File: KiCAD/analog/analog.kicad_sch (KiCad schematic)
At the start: 0 parts

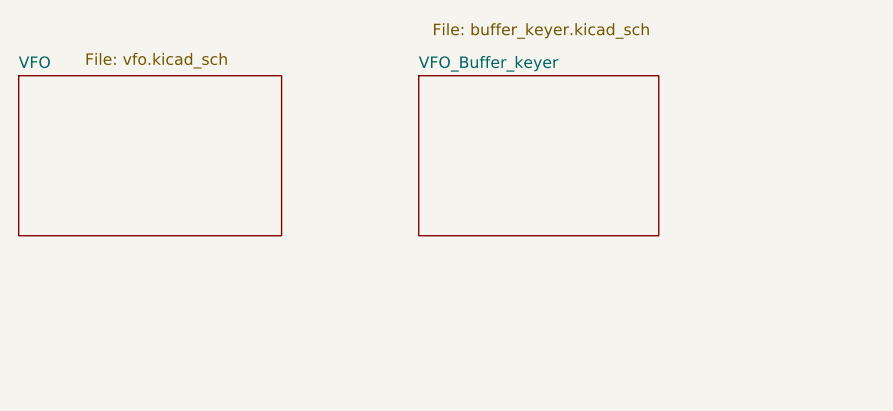
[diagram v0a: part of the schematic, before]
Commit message: KiCad revB: remove obsolete VFO sheets, add J3 footprint, add datasheets
- analog.kicad_sch: dropped VFO and VFO_Buffer_keyer sheets (legacy
  stubs superseded by VFO_Complete). Underlying vfo.kicad_sch and
  buffer_keyer.kicad_sch files deleted. PCB and .kicad_pro refreshed
  to match after Update PCB from Schematic.
- vfo_complete.kicad_sch: J3 (AC input to the +/-12V bridge) gets
  Phoenix Contact MKDS 1,5/2 footprint and a link to the local
  datasheet copy.
- Documentation/Components/: local datasheet copies for parts in the
  current supply bring-up (LM317L, LT1054, LM7800 series, 1N5817,
  2N3904/6, Kemet MLCC leaded, Phoenix Contact 142RHS).
- Documentation/Capacitors_Ordered.xlsx: capacitor inventory summary
  compiled from the Mouser and Digi-Key invoices, for stock-consistent
  reordering.

Co-Authored-By: Claude Opus 4.7 <noreply@anthropic.com>
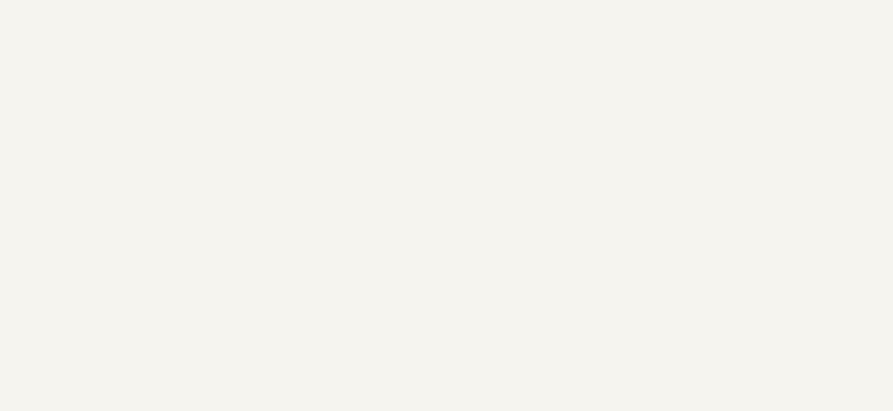
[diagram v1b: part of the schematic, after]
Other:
- removed sheet VFO
- removed sheet VFO_Buffer_keyer
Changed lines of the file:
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@@
-		)
-	)
-	(sheet
-		(at 74.93 41.91)
-		(size 26.67 17.78)
-		(exclude_from_sim no)
-		(in_bom yes)
-		(on_board yes)
-		(dnp no)
-		(stroke
-			(width 0.1524)
-			(type solid)
-		)
-		(fill
-			(color 0 0 0 0)
-		)
-		(property "Sheetname" "VFO_Buffer_keyer"
-			(at 74.93 41.1984 0)
-			(show_name no)
-			(do_not_autoplace no)
-			(effects
-				(font
-					(size 1.27 1.27)
-				)
-				(justify left bottom)
-			)
-		)
-		(property "Sheetfile" "buffer_keyer.kicad_sch"
-			(at 76.454 36.068 0)
-			(show_name no)
-			(do_not_autoplace no)
-			(effects
-				(font
-					(size 1.27 1.27)
-				)
-				(justify left top)
-			)
-		)
-		(instances
-			(project "analog"
-				(path "/d3de40b8-856b-4fbd-829c-f45ffcd55742"
-					(page "4")
-				)
-			)
-		)
-	)
-	(sheet
-		(at 30.48 41.91)
-		(size 29.21 17.78)
-		(exclude_from_sim no)
-		(in_bom yes)
-		(on_board yes)
-		(dnp no)
-		(stroke
-			(width 0.1524)
-			(type solid)
-		)
-		(fill
-			(color 0 0 0 0)
-		)
-		(property "Sheetname" "VFO"
-			(at 30.48 41.1984 0)
-			(show_name no)
-			(do_not_autoplace no)
-			(effects
-				(font
-					(size 1.27 1.27)
-				)
-				(justify left bottom)
-			)
-		)
-		(property "Sheetfile" "vfo.kicad_sch"
-			(at 37.846 39.37 0)
-			(show_name no)
-			(do_not_autoplace no)
-			(effects
-				(font
-					(size 1.27 1.27)
-				)
-				(justify left top)
-			)
-		)
-		(instances
-			(project "analog"
-				(path "/d3de40b8-856b-4fbd-829c-f45ffcd55742"
-					(page "3")
-				)
-			)
 		)
 	)

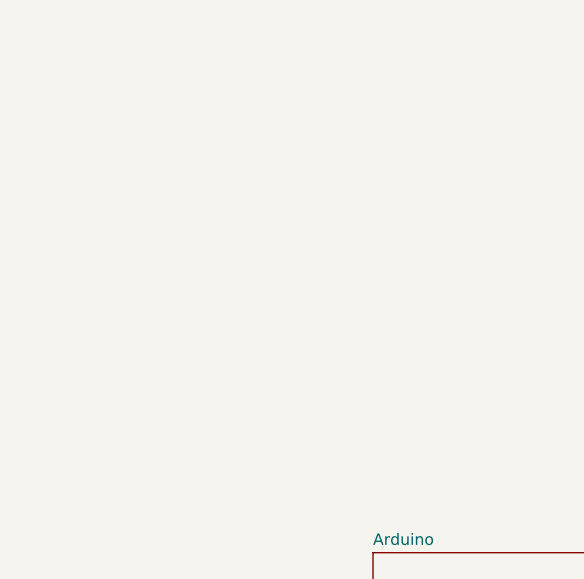
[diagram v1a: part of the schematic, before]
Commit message: revB frozen state: MCP4922 swap + LDAC decouple + sheet rename + protoshield work
Captures the in-flight state of revB at the point where the project pivoted
to a full-SS output stage on a new branch (SS_Rev_C, cut from this commit).
revB is retained as a fallback if the SS PA plan on revC proves inadequate.

Included changes:
- Analog: MCP4921 (single DAC) replaced with MCP4922 (dual DAC). Channel
  assignment: DAC_A -> PA_OUTPUT_LEVEL (new global label, awaiting PA
  board), DAC_B -> Gate 2 (DGFET envelope keyer). Channels swapped from
  initial-design intent for layout convenience.
- Analog: DAC_LDAC_N decoupled from PCF8575 P5 (that global label renamed
  to PCF_P5_SPARE). Intent: route LDAC to Metro A4 for zero-latency
  simultaneous-DAC-update capability. Physical route to A4 NOT yet added
  -- DAC_LDAC_N label on dac.kicad_sch is dangling and will fail ERC.
- Analog: KiCad-driven used_designators bookkeeping (analog.kicad_pro).
- Sheet rename: KiCAD/analog/untitled.kicad_sch -> dac.kicad_sch. Root
  schematic Sheetfile reference updated.
- Protoshield: 537 lines of additions to protoshield.kicad_sch (user
  work). Not reviewed in this commit -- carried forward as-is.
- .gitignore: added tools/_*.py exclusion (local review-helper scripts).

**revB is NOT fab-ready in this state.** See memory
project_revB_pre_fab_check.md (outside repo) for the punch list. If the
SS PA plan ever reverses and someone revives revB, ALL open items must
be closed and a full pass through Documentation/pcb_fab_checklist.md
must be completed before any gerber submit.

Co-Authored-By: Claude Opus 4.7 <noreply@anthropic.com>
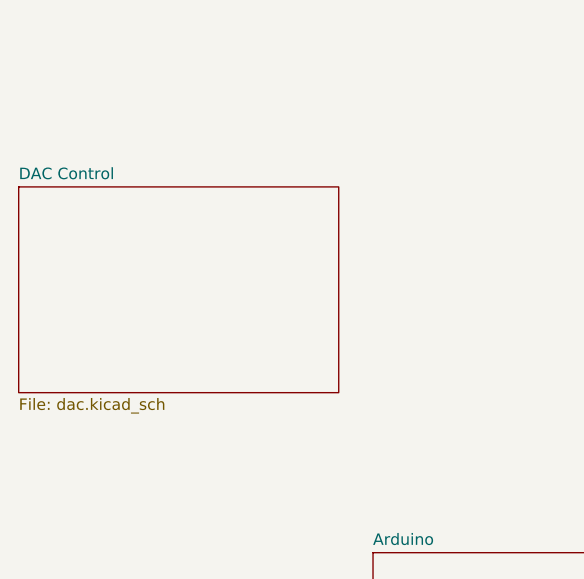
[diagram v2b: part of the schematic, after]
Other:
- added sheet DAC Control (dac.kicad_sch)
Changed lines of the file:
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@@
+		)
+	)
+	(sheet
+		(at 50.8 66.04)
+		(size 35.56 22.86)
+		(exclude_from_sim no)
+		(in_bom yes)
+		(on_board yes)
+		(dnp no)
+		(fields_autoplaced yes)
+		(stroke
+			(width 0.1524)
+			(type solid)
+		)
+		(fill
+			(color 0 0 0 0)
+		)
+		(property "Sheetname" "DAC Control"
+			(at 50.8 65.3284 0)
+			(show_name no)
+			(do_not_autoplace no)
+			(effects
+				(font
+					(size 1.27 1.27)
+				)
+				(justify left bottom)
+			)
+		)
+		(property "Sheetfile" "dac.kicad_sch"
+			(at 50.8 89.4846 0)
+			(show_name no)
+			(do_not_autoplace no)
+			(effects
+				(font
+					(size 1.27 1.27)
+				)
+				(justify left top)
+			)
+		)
+		(instances
+			(project "analog"
+				(path "/d3de40b8-856b-4fbd-829c-f45ffcd55742"
+					(page "3")
+				)
+			)
 		)
 	)

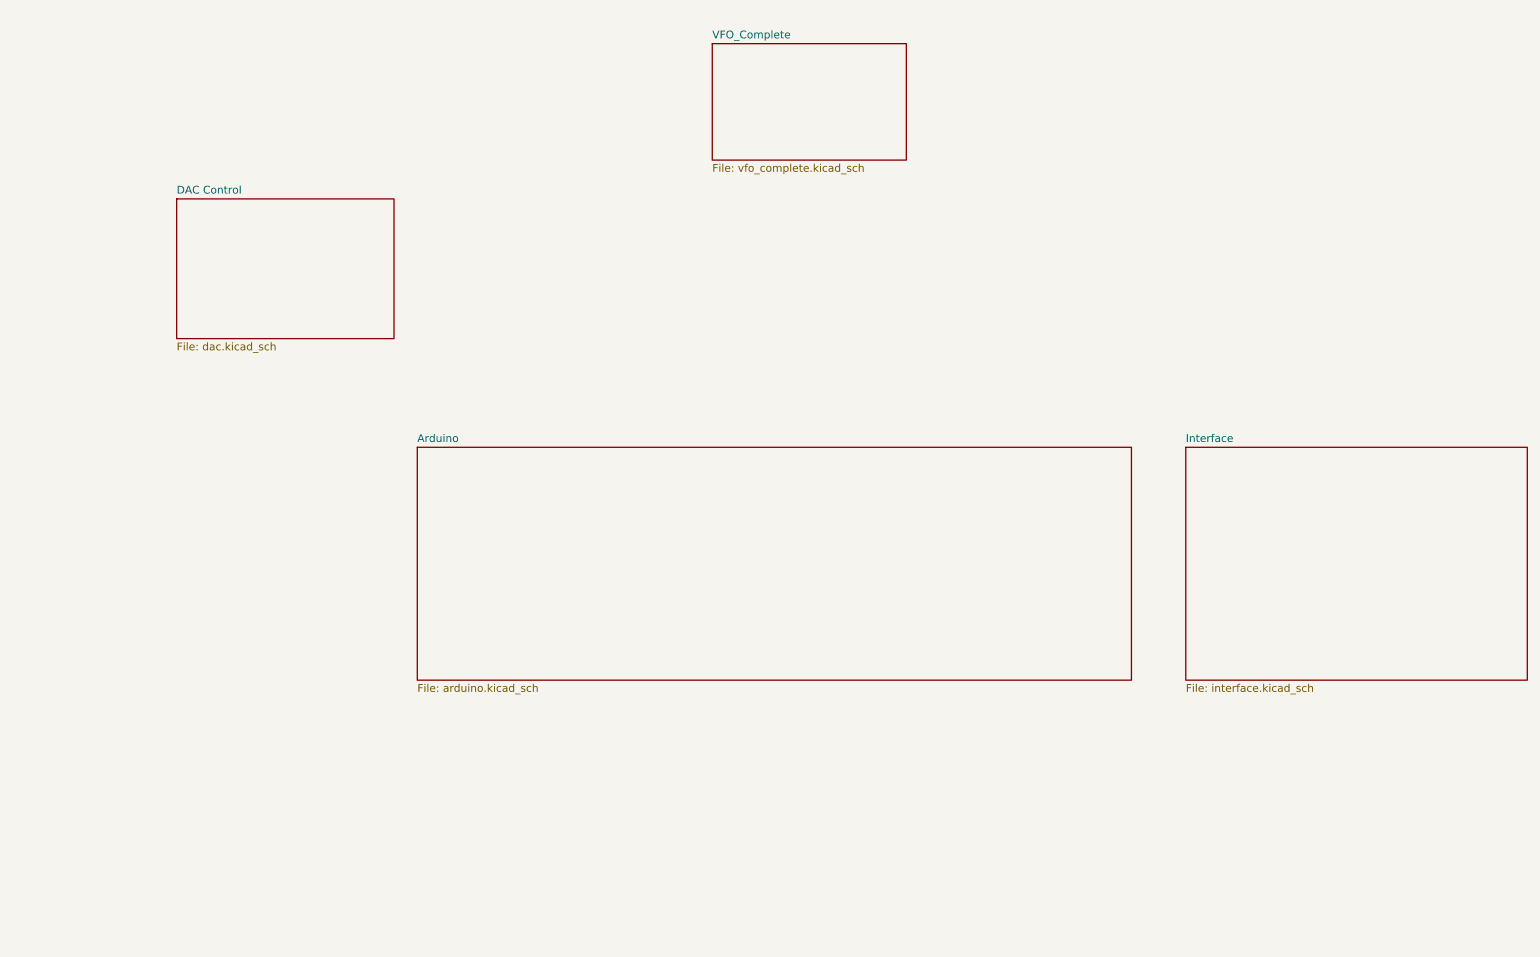
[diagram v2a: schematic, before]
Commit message: KiCad revC: RSS-SR042P relay symbol+footprint + analog multi-band stubs
Adds the junk-box RelComm RSS-SR042P SPST RF reed relay to the
project library (symbol + custom footprint) and scaffolds empty
sub-sheets on the analog board for the planned 4-band
relay-switched LPF bank and power stages.

Symbol (xmitter.kicad_sym -> Relay_SPST_RSS-SR042P):
  3 pins: RF_A, RF_B, SHIELD.  No coil pins -- coil connects
  externally via a per-relay 2-pin screw terminal placed
  elsewhere on the PCB (user plan: cut off the yellow latching
  connector and clamp bare wires into the screw terminal).

Footprint (xmitter.pretty/Relay_SPST_RelComm_RSS-SR042P.kicad_mod):
  25.4 x 8.64 mm ground base pad (relay body is grounded via
  solder joint to this pad), 2x RF signal landing pads at
  +-16 mm (jumper wires from the pads to the elevated axial RF
  pin tips), 2x 4.0 mm NPTH mounting holes at 0.68 in spacing
  oversized for 6-32 clearance.  F.Fab shows the coil housing
  as a one-sided fat-T stem (14.48 x 17.78 mm) overhanging the
  NEAR long edge of the base -- courtyard reserves that zone
  so other components can still pack tight against the FAR
  long edge.

Analog board scaffolding:
  - lpf.kicad_sch: empty sub-sheet for the 4-band LPF bank
  - power.kicad_sch: empty sub-sheet for power stages
  - analog.kicad_sch / analog.kicad_pro: top-level sheet
    references + project config entries

Not yet done: schematic contents of lpf.kicad_sch and power.kicad_sch
(including the paralleled-input / output-only-relay-switched topology
discussed, with upstream op-amp buffer feeding the 4 LPFs and only
the output path relay-switched).

Co-Authored-By: Claude Opus 4.7 <noreply@anthropic.com>
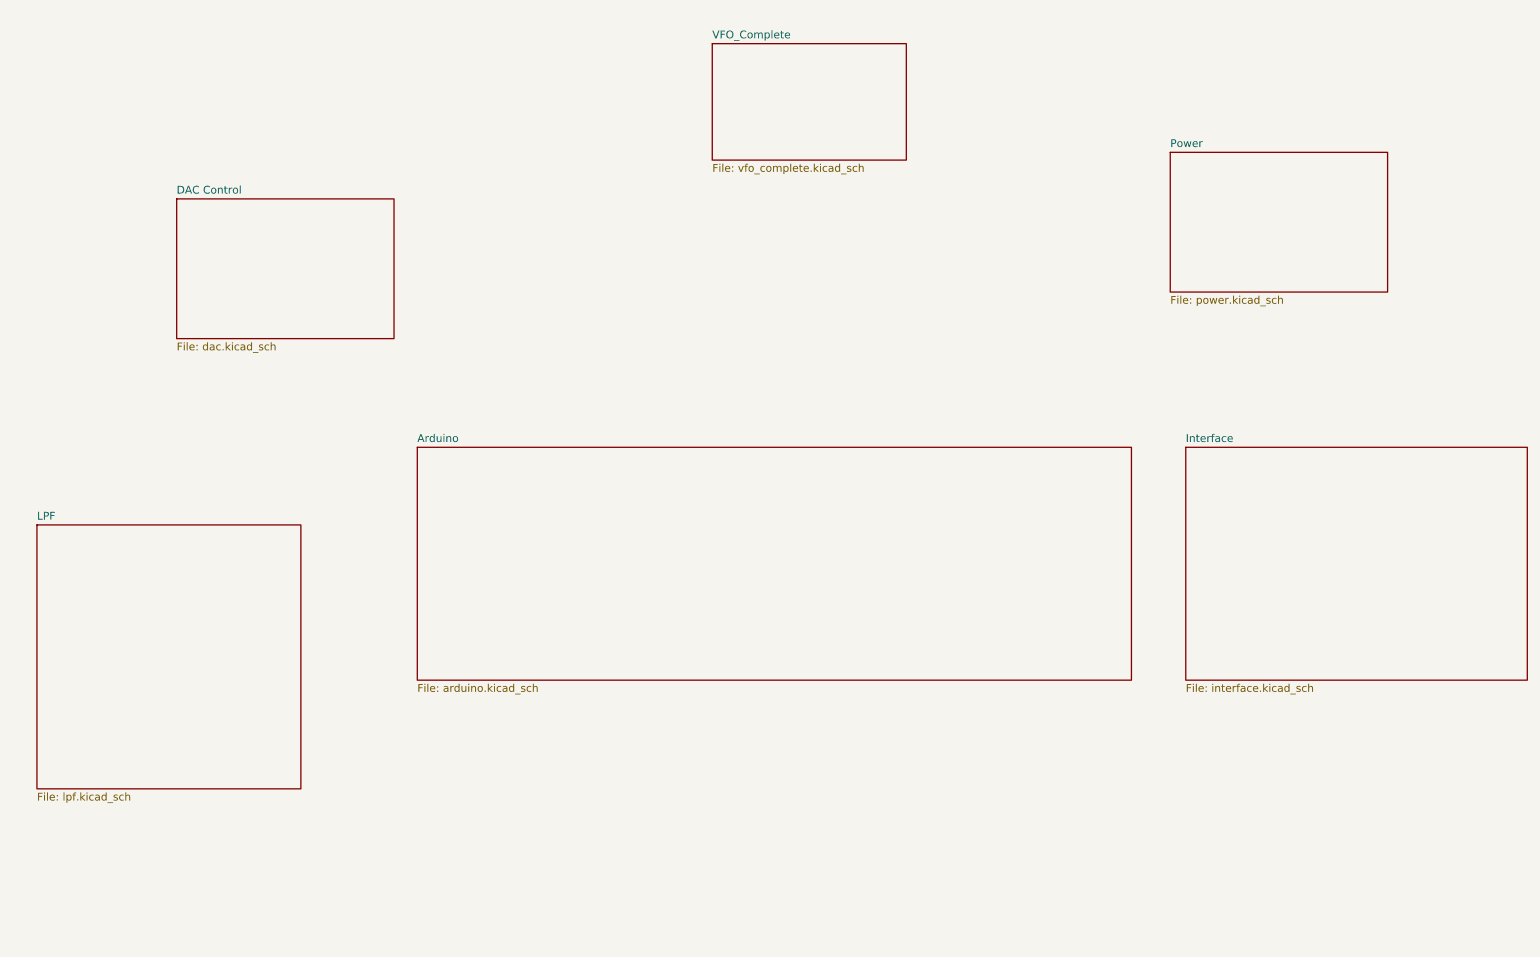
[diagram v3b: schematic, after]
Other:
- added sheet LPF (lpf.kicad_sch)
- added sheet Power (power.kicad_sch)
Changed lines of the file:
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@@
+	)
+	(sheet
+		(at 213.36 58.42)
+		(size 35.56 22.86)
+		(exclude_from_sim no)
+		(in_bom yes)
+		(on_board yes)
+		(dnp no)
+		(fields_autoplaced yes)
+		(stroke
+			(width 0.1524)
+			(type solid)
+		)
+		(fill
+			(color 0 0 0 0)
+		)
+		(property "Sheetname" "Power"
+			(at 213.36 57.7084 0)
+			(show_name no)
+			(do_not_autoplace no)
+			(effects
+				(font
+					(size 1.27 1.27)
+				)
+				(justify left bottom)
+			)
+		)
+		(property "Sheetfile" "power.kicad_sch"
+			(at 213.36 81.8646 0)
+			(show_name no)
+			(do_not_autoplace no)
+			(effects
+				(font
+					(size 1.27 1.27)
+				)
+				(justify left top)
+			)
+		)
+		(instances
+			(project "analog"
+				(path "/d3de40b8-856b-4fbd-829c-f45ffcd55742"
+					(page "6")
+				)
+			)
+		)
+	)
+	(sheet
+		(at 27.94 119.38)
+		(size 43.18 43.18)
+		(exclude_from_sim no)
+		(in_bom yes)
+		(on_board yes)
+		(dnp no)
+		(fields_autoplaced yes)
+		(stroke
+			(width 0.1524)
+			(type solid)
+		)
+		(fill
+			(color 0 0 0 0)
+		)
+		(property "Sheetname" "LPF"
+			(at 27.94 118.6684 0)
+			(show_name no)
+			(do_not_autoplace no)
+			(effects
+				(font
+					(size 1.27 1.27)
+				)
+				(justify left bottom)
+			)
+		)
+		(property "Sheetfile" "lpf.kicad_sch"
+			(at 27.94 163.1446 0)
+			(show_name no)
+			(do_not_autoplace no)
+			(effects
+				(font
+					(size 1.27 1.27)
+				)
+				(justify left top)
+			)
+		)
+		(instances
+			(project "analog"
+				(path "/d3de40b8-856b-4fbd-829c-f45ffcd55742"
+					(page "4")
+				)
+			)
+		)
 	)
 	(sheet

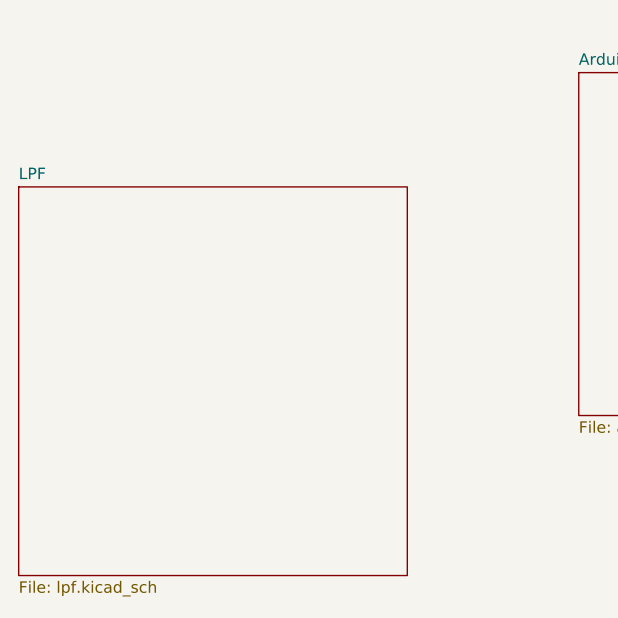
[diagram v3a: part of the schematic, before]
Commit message: revD: drop stale LPF sub-sheets from analog + ss_pa, scrub 13.8V text comments
- Remove hierarchical LPF sub-sheets from analog and ss_pa roots; LPF
  now lives in its own project (KiCAD/Output LPF/).
- Delete the skeleton lpf.kicad_sch files and corresponding entries
  from both .kicad_pro sheet-UUID lists.
- Scrub two stale text annotations on analog/power.kicad_sch:
  "13.8V in" -> "Shack supply in" and the J5/J33/J34 legend box.
  13.8V now only appears on ss_pa and the shared +13.8V power-symbol
  definition in xmitter.kicad_sym.

Co-Authored-By: Claude Opus 4.7 <noreply@anthropic.com>
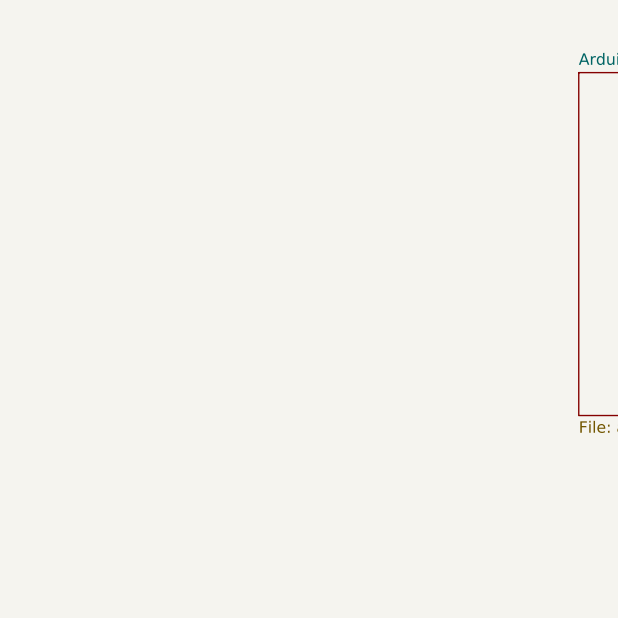
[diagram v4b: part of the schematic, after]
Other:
- removed sheet LPF
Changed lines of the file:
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@@
-	)
-	(sheet
-		(at 27.94 119.38)
-		(size 43.18 43.18)
-		(exclude_from_sim no)
-		(in_bom yes)
-		(on_board yes)
-		(dnp no)
-		(fields_autoplaced yes)
-		(stroke
-			(width 0.1524)
-			(type solid)
-		)
-		(fill
-			(color 0 0 0 0)
-		)
-		(property "Sheetname" "LPF"
-			(at 27.94 118.6684 0)
-			(show_name no)
-			(do_not_autoplace no)
-			(effects
-				(font
-					(size 1.27 1.27)
-				)
-				(justify left bottom)
-			)
-		)
-		(property "Sheetfile" "lpf.kicad_sch"
-			(at 27.94 163.1446 0)
-			(show_name no)
-			(do_not_autoplace no)
-			(effects
-				(font
-					(size 1.27 1.27)
-				)
-				(justify left top)
-			)
-		)
-		(instances
-			(project "analog"
-				(path "/d3de40b8-856b-4fbd-829c-f45ffcd55742"
-					(page "4")
-				)
-			)
-		)
 	)
 	(sheet
